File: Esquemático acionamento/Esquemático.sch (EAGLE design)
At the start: 9 parts, among them Q1 IRF540, Q2 IRF540

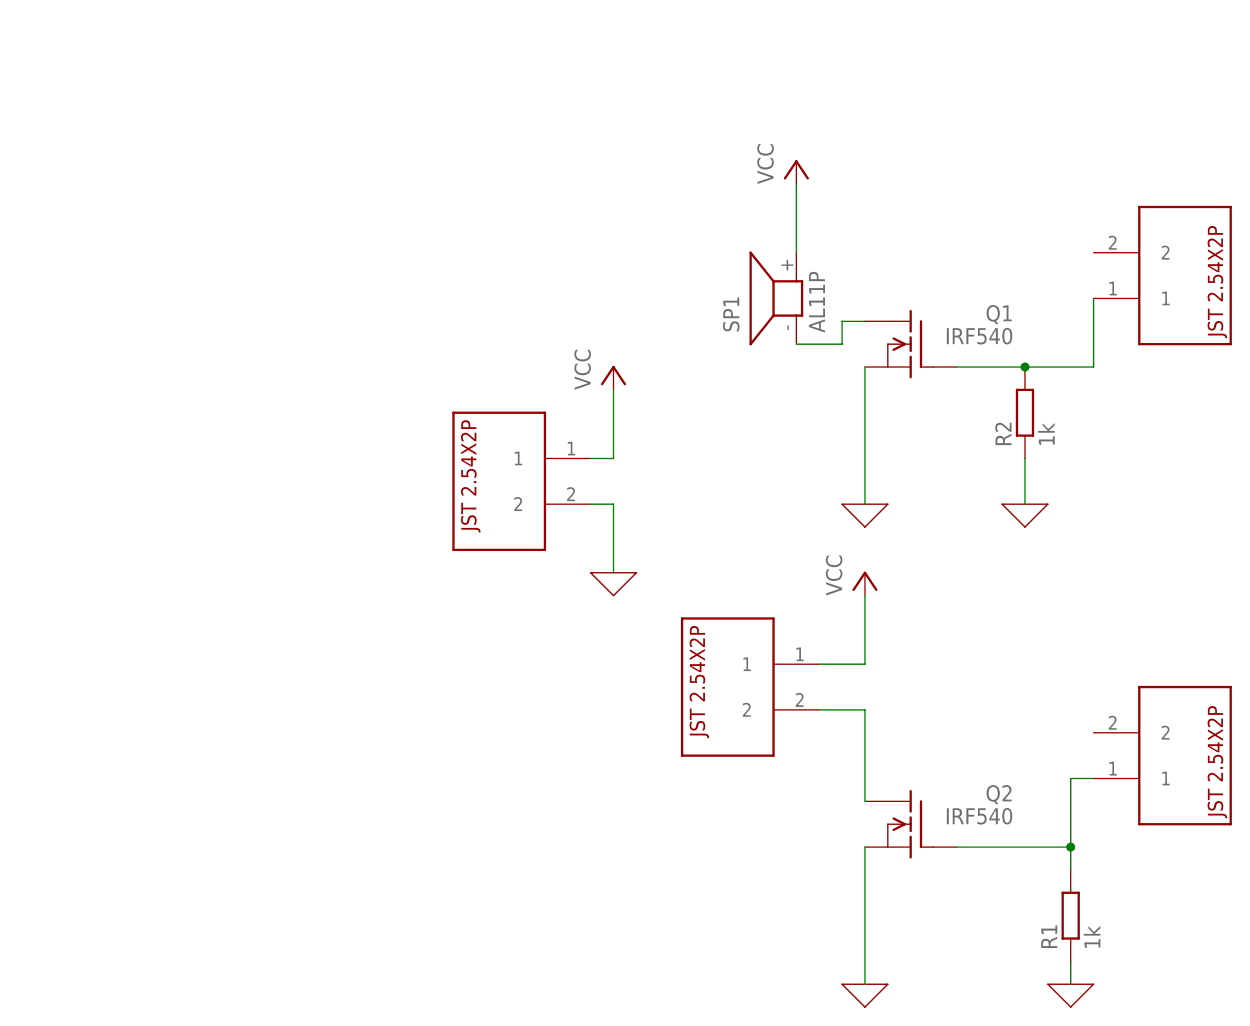
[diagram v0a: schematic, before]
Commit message: Melhorei a placa de acionamento
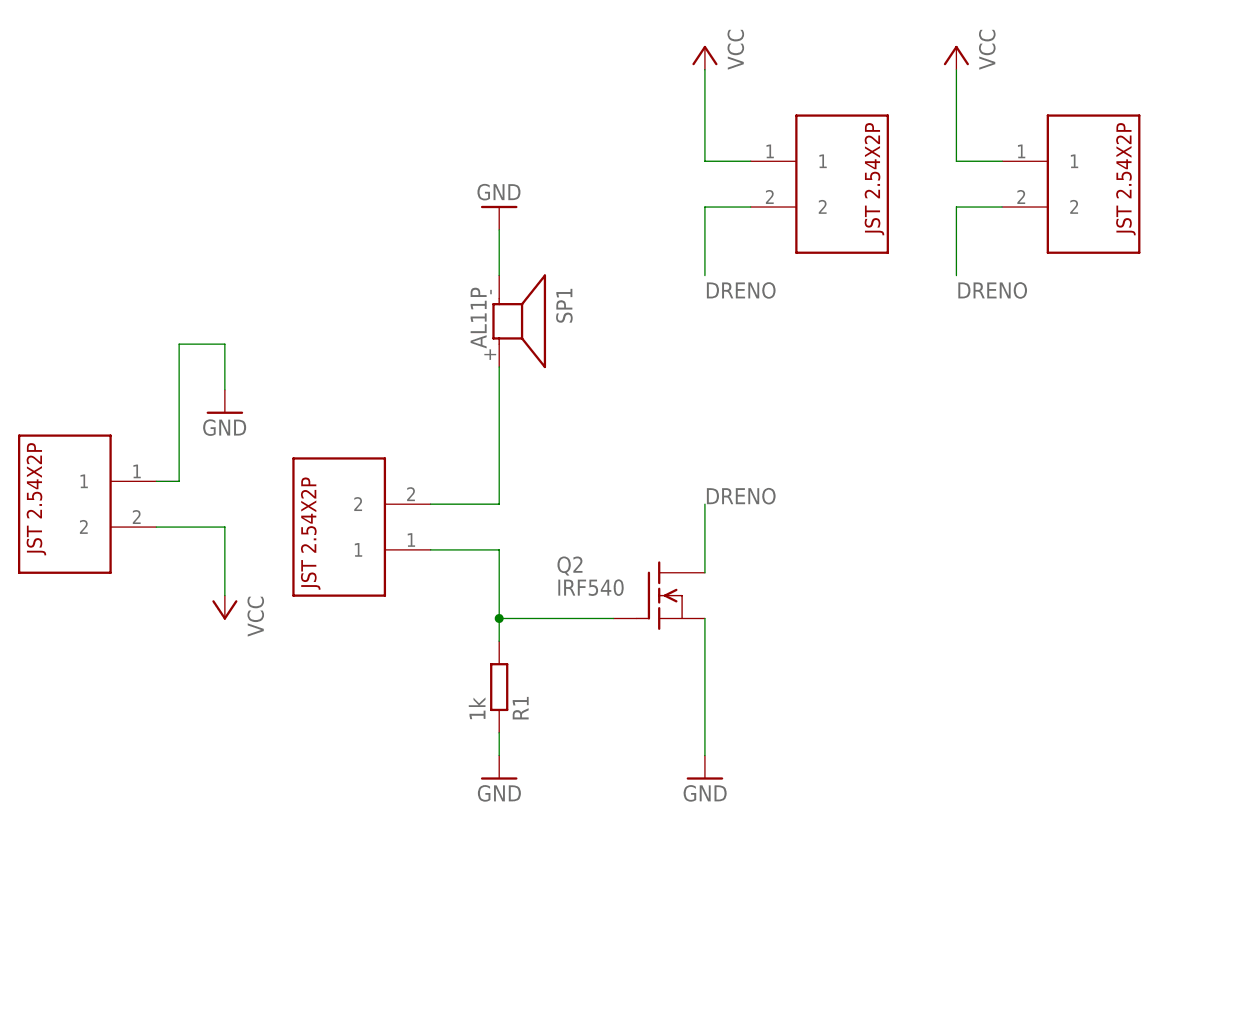
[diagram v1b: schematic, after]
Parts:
- removed Q1: IRF540, transistor-fet:IRF540
- removed R2: 1k, rcl:R-EU_0204/7
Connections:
- removed net 0: Q1.S, Q2.S, R1.1, R2.1, U$4.2
- removed net N$2: Q2.D, U$2.2
- removed net N$4: U$2.1
- removed net N$5: Q1.D, SP1.1
- new net DRENO: Q2.D, U$2.2, U$3.2
- new net GND: Q2.S, R1.1, SP1.1, U$4.1
- net N$3: now also SP1.2, U$1.2; no longer Q1.G, R2.2, U$3.1
- net VCC: now also U$2.1, U$3.1, U$4.2; no longer SP1.2, U$4.1
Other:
- moved on the sheet: Q2, R1, SP1
